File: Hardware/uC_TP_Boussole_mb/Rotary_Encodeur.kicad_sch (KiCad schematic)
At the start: 11 parts, among them SW4 RotaryEncoder_Switch

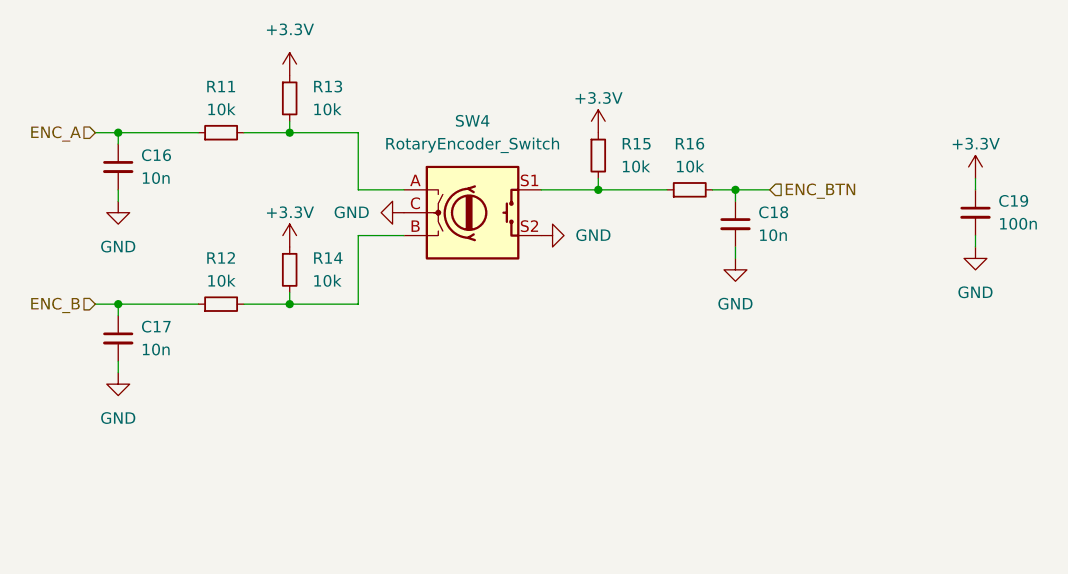
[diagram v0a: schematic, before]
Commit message: starting pin out nucleo
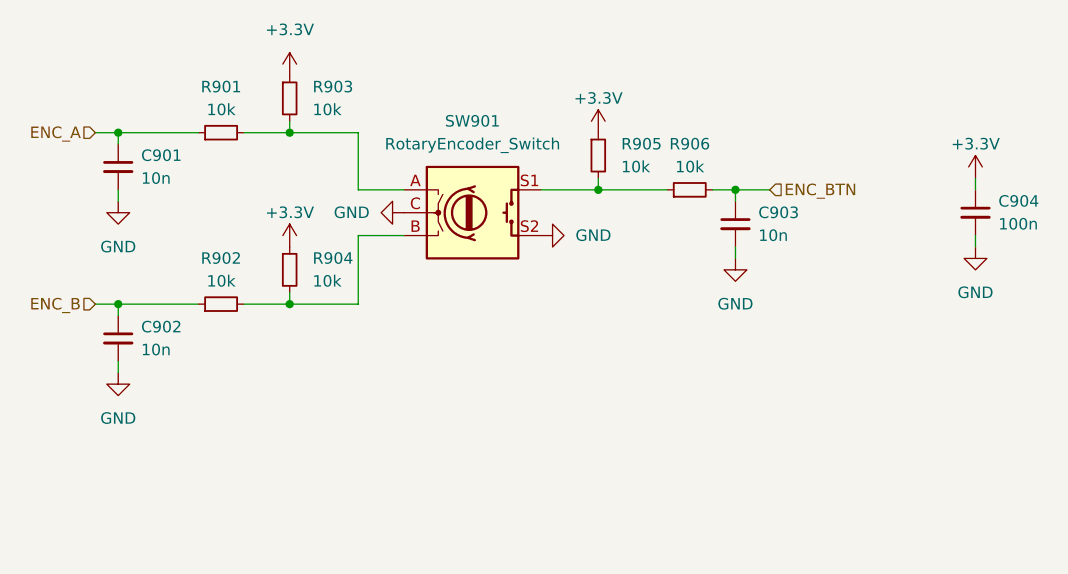
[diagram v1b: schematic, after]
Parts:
- C901: renamed from C16; footprint (none) -> Capacitor_SMD:C_0402_1005Metric
- C902: renamed from C17; footprint (none) -> Capacitor_SMD:C_0402_1005Metric
- C903: renamed from C18; footprint (none) -> Capacitor_SMD:C_0402_1005Metric
- C904: renamed from C19; footprint (none) -> Capacitor_SMD:C_0402_1005Metric
- R901: renamed from R11; footprint (none) -> Resistor_SMD:R_0402_1005Metric
- R902: renamed from R12; footprint (none) -> Resistor_SMD:R_0402_1005Metric
- R903: renamed from R13; footprint (none) -> Resistor_SMD:R_0402_1005Metric
- R904: renamed from R14; footprint (none) -> Resistor_SMD:R_0402_1005Metric
- R905: renamed from R15; footprint (none) -> Resistor_SMD:R_0402_1005Metric
- R906: renamed from R16; footprint (none) -> Resistor_SMD:R_0402_1005Metric
- renumbered SW4 to SW901

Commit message: update schematic
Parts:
- SW901: MPN (none) -> 482016514001
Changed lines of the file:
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@@
 			)
 		)
-		(property "Datasheet" "~"
+		(property "Datasheet" "https://www.we-online.com/components/products/datasheet/482016514001.pdf"
 			(at 64.77 53.086 0)
 			(effects
@@
 			(at 64.77 59.69 0)
 			(effects
+				(font
+					(size 1.27 1.27)
+				)
+				(hide yes)
+			)
+		)
+		(property "MPN" "482016514001"
+			(at 64.77 59.69 0)
+			(effects

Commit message: ddd
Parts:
- SW901: footprint (none) -> libs:482016514001_Mechanical_Incremental_Encoder_Switch
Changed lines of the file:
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@@
 			)
 		)
-		(property "Footprint" ""
+		(property "Footprint" "libs:482016514001_Mechanical_Incremental_Encoder_Switch"
 			(at 60.96 55.626 0)
 			(effects

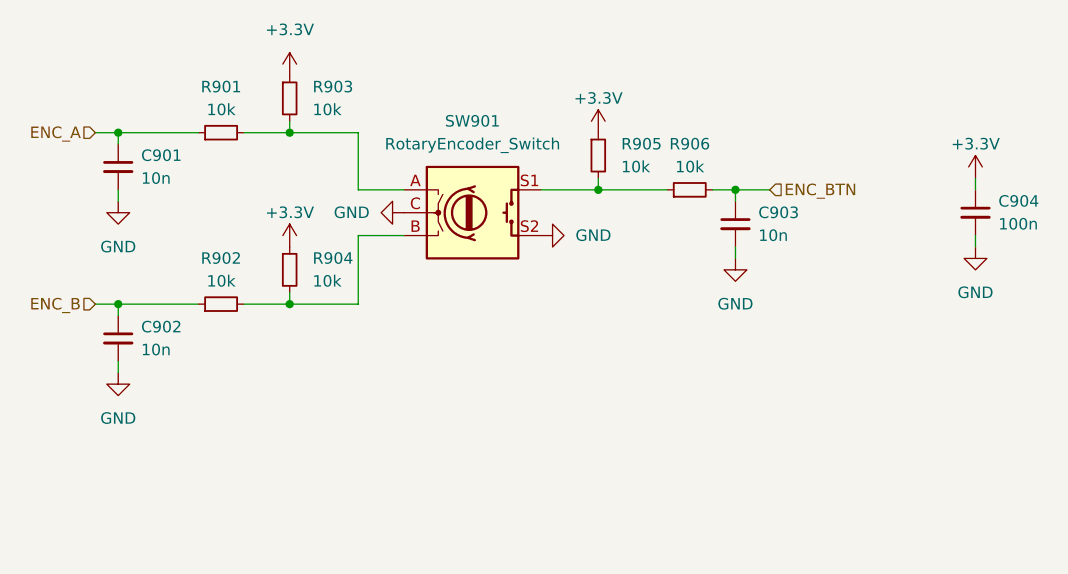
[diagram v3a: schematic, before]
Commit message: update schematic
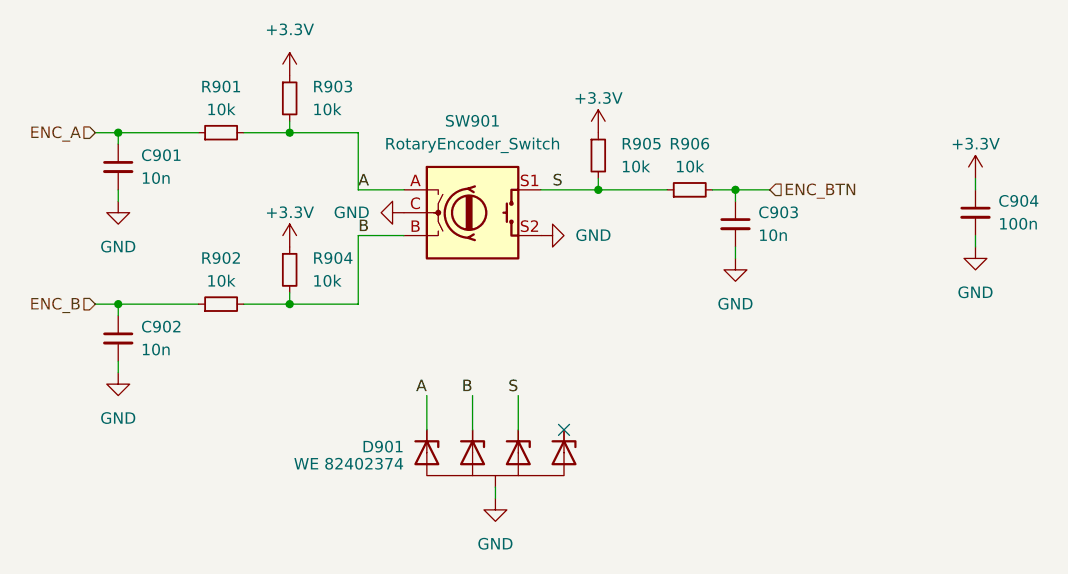
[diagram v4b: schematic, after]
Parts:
- added D901: WE 82402374, libs:SC70-5L, symbol mylibs:D_TVS_Uni_x4
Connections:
- net GND: now also D901.2 (GND)
- net A: now reaches R901.2, R903.2, SW901.A
- net A: now also D901.5 (I/O)
- net B: now reaches R902.2, R904.2, SW901.B
- net B: now also D901.4 (I/O)
- net S: now reaches R905.2, R906.1, SW901.S1
- net S: now also D901.3 (I/O)
- no-connect marks 0 -> 1

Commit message: finalize pcb
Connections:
- net S: now also D901.1 (I/O); no longer D901.3 (I/O)
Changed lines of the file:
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@@
 	)
 	(no_connect
-		(at 74.93 83.82)
+		(at 69.85 83.82)
 	)
 	(wire
@@
 	(wire
 		(pts
+			(xy 74.93 80.01) (xy 74.93 83.82)
+		)
+		(stroke
+			(width 0)
+			(type default)
+		)
+	)
+	(wire
+		(pts
 			(xy 52.07 62.23) (xy 52.07 69.85)
 		)
@@
 		(pts
 			(xy 22.86 50.8) (xy 25.4 50.8)
-		)
-		(stroke
-			(width 0)
-			(type default)
-		)
-	)
-	(wire
-		(pts
-			(xy 69.85 80.01) (xy 69.85 83.82)
 		)
 		(stroke
@@
 		)
 	)
+	(label "S"
+		(at 74.93 80.01 180)
+		(fields_autoplaced yes)
+		(effects
+			(font
+				(size 1.27 1.27)
+			)
+			(justify right bottom)
+		)
+	)
 	(label "B"
 		(at 52.07 62.23 0)
@@
 		(fields_autoplaced yes)
 		(effects
-			(font
-				(size 1.27 1.27)
-			)
-			(justify right bottom)
-		)
-	)
-	(label "S"
-		(at 69.85 80.01 180)
-		(fields_autoplaced yes)
-		(effects

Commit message: bom
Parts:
- SW901: MPN 482016514001 -> WE 482016514001
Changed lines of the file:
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@@
 			)
 		)
-		(property "MPN" "482016514001"
+		(property "MPN" "WE 482016514001"
 			(at 64.77 59.69 0)
 			(effects
